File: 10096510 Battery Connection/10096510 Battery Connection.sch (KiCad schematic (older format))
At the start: 27 parts, among them J1 09185107323, J3 811-S1-002-30-014101, J4 811-S1-002-30-014101, J5 811-S1-002-30-014101, J6 GKS-913-0024

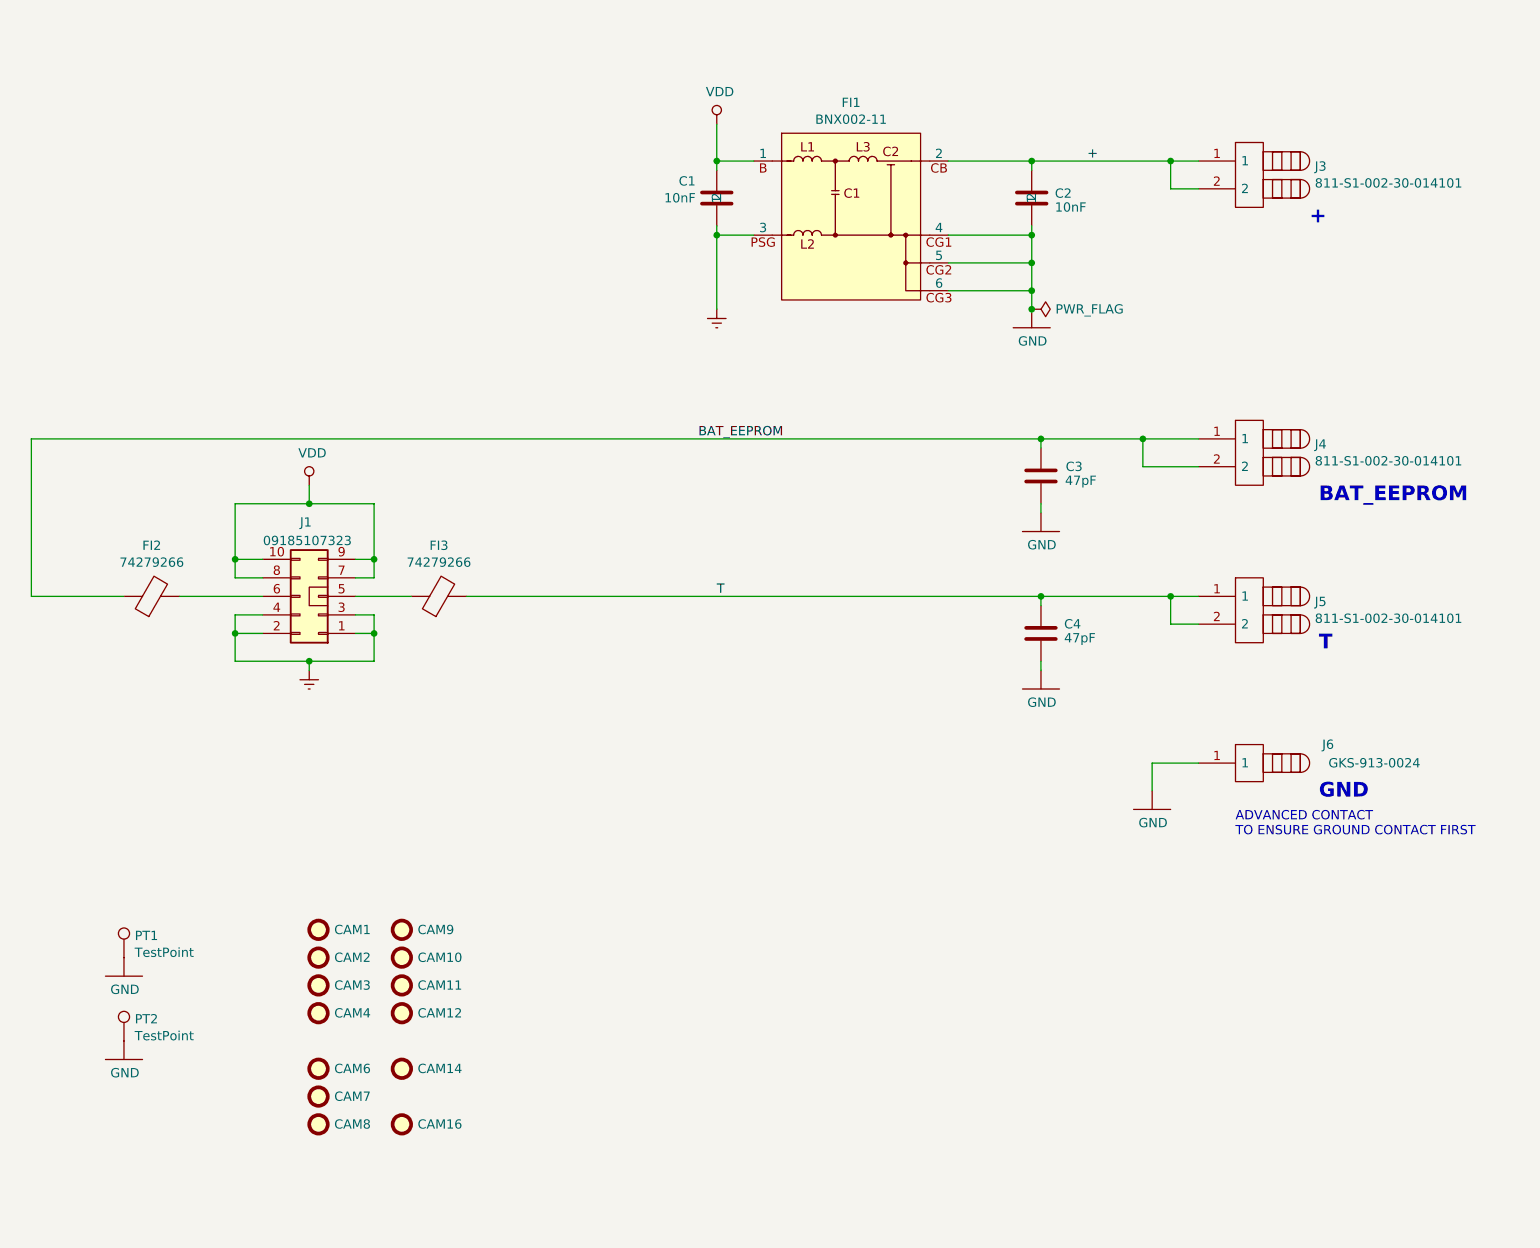
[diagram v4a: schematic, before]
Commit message: make the schematic net names match those of the Zuken PCB
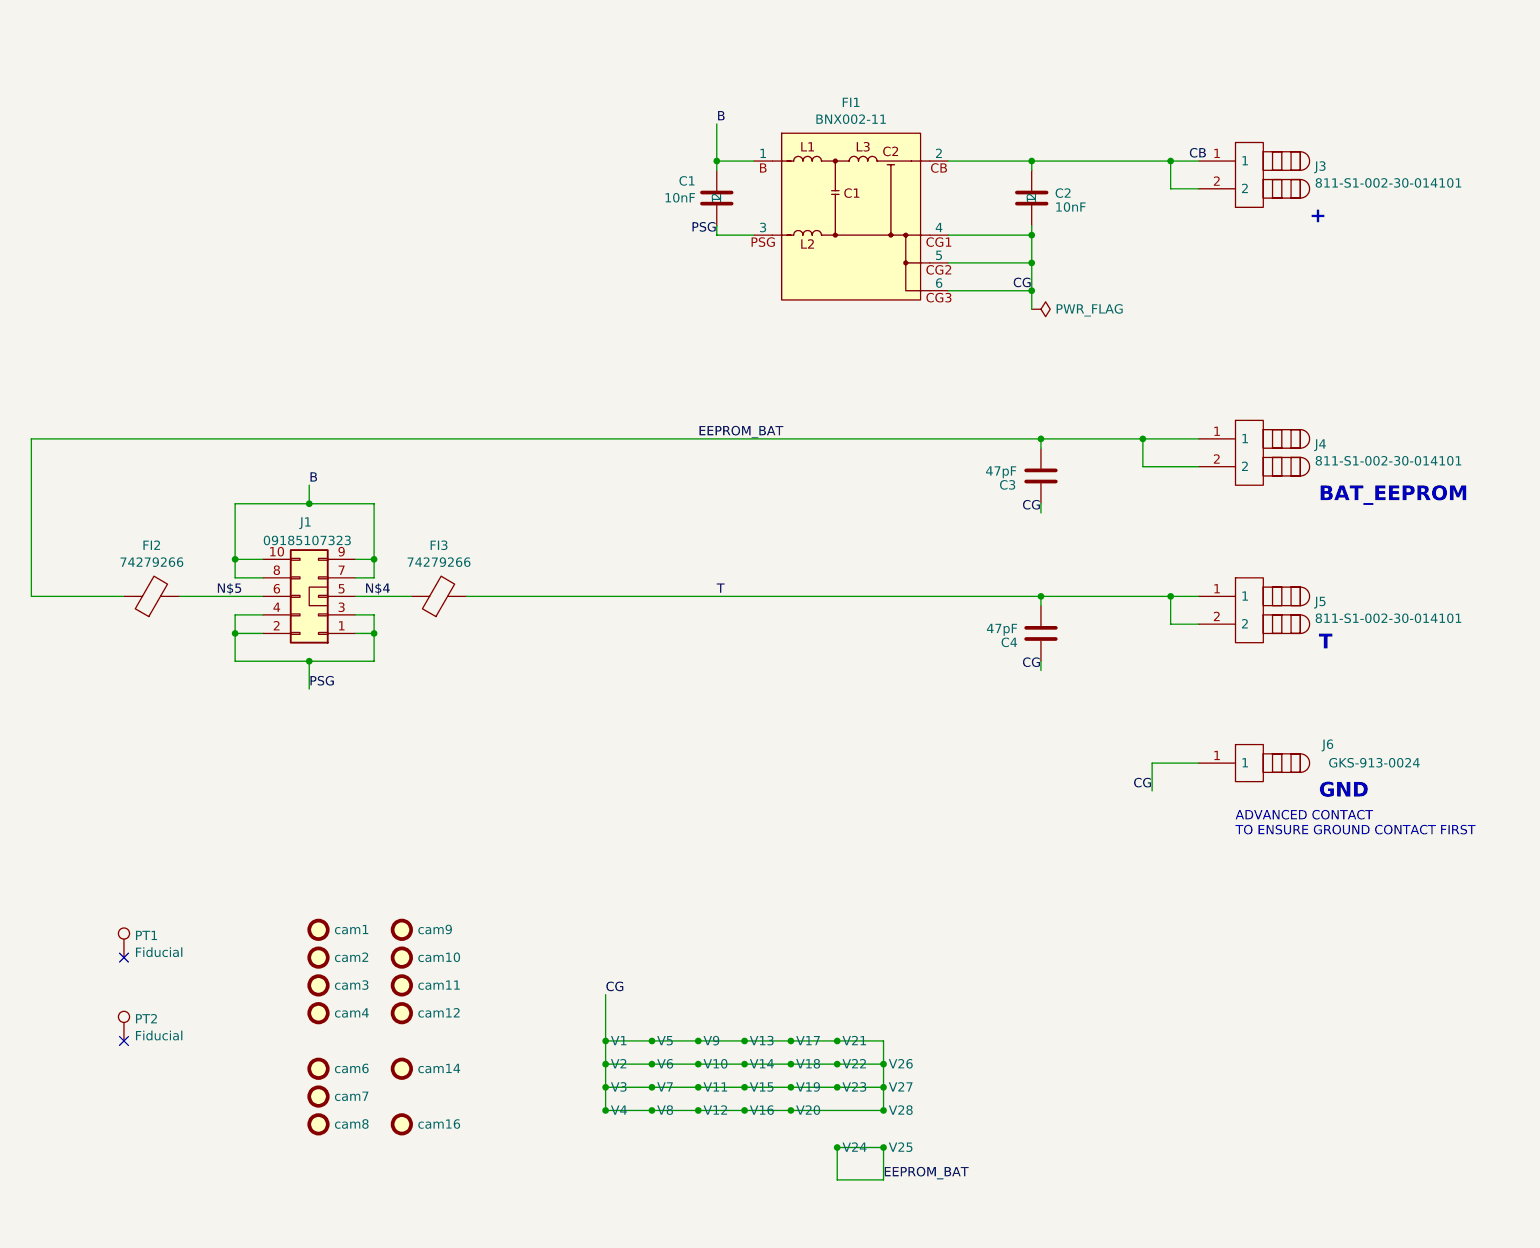
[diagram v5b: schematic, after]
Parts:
- added V1, V10, V11, V12, V13, V14, V15, V16, V17, V18, V19, V2, V20, V21, V22, V23, V24, V25, V26, V27, V28, V3, V4, V5, V6, V7, V8, V9: Via, batt:VIA-100X04-VE, symbol V_Connector:Via
- PT1, PT2: value TestPoint -> Fiducial
- cam1: renamed from CAM1; value Fiducial -> ~; footprint AllModules:FILM18_HORIZONTAL_1 -> batt:FILM18_HORIZONTAL
- cam10: renamed from CAM10; value Fiducial -> ~; footprint AllModules:A3_PER_COVIDIEN_1 -> batt:A3_PER_COVIDIEN
- cam11: renamed from CAM11; value Fiducial -> ~; footprint AllModules:FEE_COMP_2 -> batt:FEE_COMP_0.3
- cam12: renamed from CAM12; value Fiducial -> ~; footprint AllModules:FABRICATION-FEE_1 -> batt:FABRICATION-FEE
- cam14: renamed from CAM14; value Fiducial -> ~; footprint AllModules:PERCAGE-MC_TABLEAU_1 -> batt:PERCAGE-MC_TABLEAU
- cam16: renamed from CAM16; value Fiducial -> ~; footprint AllModules:FEE_COMP_1 -> batt:FEE_COMP_0.3
- cam2: renamed from CAM2; value Fiducial -> ~; footprint AllModules:A3_EQFC_COVIDIEN_1 -> batt:A3_EQFC_COVIDIEN
- cam3: renamed from CAM3; value Fiducial -> ~; footprint AllModules:PER-COVIDIEN_TEXTE_1 -> batt:PER-COVIDIEN_TEXTE
- cam4: renamed from CAM4; value Fiducial -> ~; footprint AllModules:A3_EQFS_COVIDIEN_1 -> batt:A3_EQFS_COVIDIEN
- cam6: renamed from CAM6; value Fiducial -> ~; footprint AllModules:COIN_EXTERNE_1 -> batt:COIN_EXTERNE_0.5
- cam7: renamed from CAM7; value Fiducial -> ~; footprint AllModules:COIN_EXTERNE_1 -> batt:COIN_EXTERNE_0.5
- cam8: renamed from CAM8; value Fiducial -> ~; footprint AllModules:COIN_EXTERNE_1 -> batt:COIN_EXTERNE_0.5
- cam9: renamed from CAM9; value Fiducial -> ~; footprint AllModules:COIN_EXTERNE_1 -> batt:COIN_EXTERNE_0.5
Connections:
- net T: now also C4.2; no longer C4.1
- net CG: now reaches C2.1, FI1.CG1 (4), FI1.CG2 (5), FI1.CG3 (6)
- net CG: now also C3.1, C4.1, J6.1, V1.~, V10.~, V11.~, V12.~, V13.~, V14.~, V15.~, V16.~, V17.~, V18.~, V19.~, V2.~, V20.~, V21.~, V22.~, V23.~, V26.~, V27.~, V28.~, V3.~, V4.~, V5.~, V6.~, V7.~, V8.~, V9.~
- net EEPROM_BAT: now reaches C3.2
- net EEPROM_BAT: now also FI2.1, J4.1, J4.2, V24.~, V25.~
- net N$4: now reaches FI3.1, J1.5 (Pin_5)
- net N$5: now reaches FI2.2, J1.6 (Pin_6)
- net + renamed CB
- removed net BAT_EEPROM: C3.1, FI2.1, J4.1, J4.2
- net Earth renamed PSG
- net VDD renamed B
- no-connect marks 0 -> 2

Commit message: Battery conn update for sync
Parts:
- V1, V10, V11, V12, V13, V14, V15, V16, V17, V18, V19, V2, V20, V21, V22, V23, V24, V25, V26, V27, V28, V3, V4, V5, V6, V7, V8, V9: footprint batt:VIA-100X04-VE -> AllModules:VIA-100X04-VE
- cam1: footprint batt:FILM18_HORIZONTAL -> AllModules:FILM18_HORIZONTAL
- cam10: footprint batt:A3_PER_COVIDIEN -> AllModules:A3_PER_COVIDIEN
- cam11, cam16: footprint batt:FEE_COMP_0.3 -> AllModules:FEE_COMP_0.3
- cam12: footprint batt:FABRICATION-FEE -> AllModules:FABRICATION-FEE
- cam14: footprint batt:PERCAGE-MC_TABLEAU -> AllModules:PERCAGE-MC_TABLEAU
- cam2: footprint batt:A3_EQFC_COVIDIEN -> AllModules:A3_EQFC_COVIDIEN
- cam3: footprint batt:PER-COVIDIEN_TEXTE -> AllModules:PER-COVIDIEN_TEXTE
- cam4: footprint batt:A3_EQFS_COVIDIEN -> AllModules:A3_EQFS_COVIDIEN
- cam6, cam7, cam8, cam9: footprint batt:COIN_EXTERNE_0.5 -> AllModules:COIN_EXTERNE_0.5
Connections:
- net CG is gone; now on net CB: C2.1, C3.1, C4.1, FI1.CG1 (4), FI1.CG2 (5), FI1.CG3 (6), J6.1, V1.~, V10.~, V11.~, V12.~, V13.~, V14.~, V15.~, V16.~, V17.~, V18.~, V19.~, V2.~, V20.~, V21.~, V22.~, V23.~, V26.~, V27.~, V28.~, V3.~, V4.~, V5.~, V6.~, V7.~, V8.~, V9.~
- net PSG is gone; now on net B: C1.1, FI1.PSG (3), J1.1 (Pin_1), J1.2 (Pin_2), J1.3 (Pin_3), J1.4 (Pin_4)
- net N$4: no longer names the net of FI3.1, J1.5 (Pin_5)
- net N$5: no longer names the net of FI2.2, J1.6 (Pin_6)
